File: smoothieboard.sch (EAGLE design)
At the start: 235 parts, among them IC10 LM1117-3.3V, IC2 A4982, IC3 A4982, IC4 MCP44X1, IC5 A4982, IC6 A4982, IC9 78L12Z, J10 POWER_JACKSMD, J5 POWER_JACKSMD, Q1 BC857ALT1SMD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

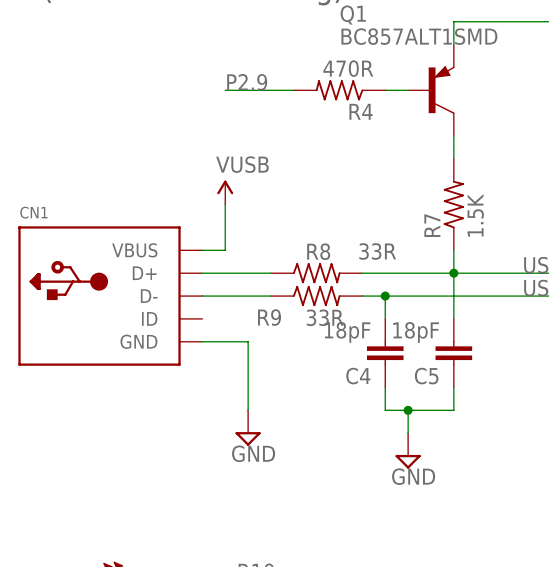
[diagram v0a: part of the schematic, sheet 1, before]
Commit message: Added USB-B Connector, other fixes
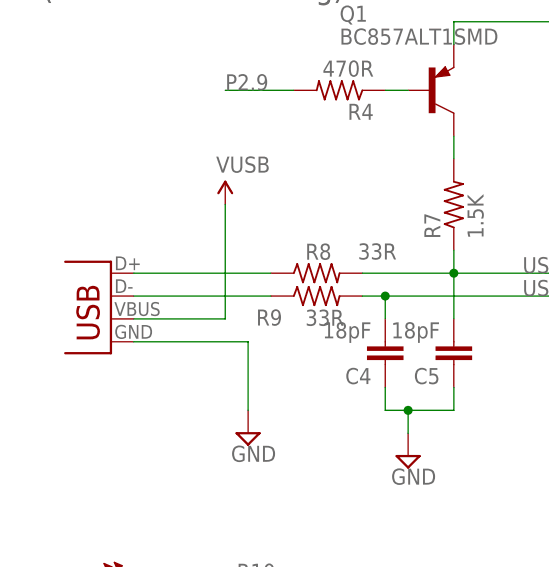
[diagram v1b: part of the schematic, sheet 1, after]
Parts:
- removed CN1: (no value), microbuilder:USBMINIB
- added X13: USBPTH, SparkFun:USBPTH
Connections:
- net GND: now also X13.GND; no longer CN1.GND
- net N$61: now also X13.D+; no longer CN1.D+
- net N$62: now also X13.D-; no longer CN1.D-
- net VUSB: now also X13.VBUS; no longer CN1.VBUS
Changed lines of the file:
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@@
 <setting verticaltext="up"/>
 </settings>
-<grid distance="0.01" unitdist="inch" unit="inch" style="lines" multiple="1" display="no" altdistance="0.01" altunitdist="inch" altunit="inch"/>
+<grid distance="0.1" unitdist="inch" unit="inch" style="lines" multiple="1" display="no" altdistance="0.01" altunitdist="inch" altunit="inch"/>
 <layers>
 <layer number="1" name="Top" color="4" fill="1" visible="no" active="no"/>
@@
 <part name="SUPPLY3" library="supply2" deviceset="GND" device=""/>
 <part name="C7" library="SparkFun" deviceset="CAP_POL" device="1206" value="10uF"/>
-<part name="CN1" library="microbuilder" deviceset="USB" device="MINIB"/>
 <part name="L1" library="SparkFun" deviceset="INDUCTOR" device="0603"/>
 <part name="SUPPLY25" library="supply2" deviceset="GND" device=""/>
@@
 <part name="JP31" library="SparkFun" deviceset="JUMPER-2" device="SMD-NC"/>
 <part name="U$2" library="custom_esorensen" deviceset="TC4427" device=""/>
+<part name="X13" library="SparkFun" deviceset="USB" device="PTH"/>
 </parts>
 <sheets>
@@
 <instance part="SUPPLY3" gate="GND" x="264.16" y="83.82"/>
 <instance part="C7" gate="G$1" x="302.26" y="96.52"/>
-<instance part="CN1" gate="G$1" x="20.32" y="149.86"/>
 <instance part="L1" gate="G$1" x="254" y="106.68" rot="R90"/>
 <instance part="SUPPLY25" gate="GND" x="226.06" y="106.68"/>
@@
 <instance part="JP15" gate="G$1" x="294.64" y="124.46" rot="R180"/>
 <instance part="JP29" gate="G$1" x="73.66" y="104.14" rot="R180"/>
+<instance part="X13" gate="G$1" x="20.32" y="144.78" rot="MR0"/>
 </instances>
 <busses>
@@
 </segment>
 <segment>
-<wire x1="30.48" y1="144.78" x2="35.56" y2="144.78" width="0.1524" layer="91"/>
 <wire x1="35.56" y1="144.78" x2="35.56" y2="137.16" width="0.1524" layer="91"/>
-<pinref part="CN1" gate="G$1" pin="GND"/>
 <pinref part="SUPPLY28" gate="GND" pin="GND"/>
+<pinref part="X13" gate="G$1" pin="GND"/>
+<wire x1="35.56" y1="144.78" x2="22.86" y2="144.78" width="0.1524" layer="91"/>
 </segment>
 <segment>
@@
 <net name="N$61" class="0">
 <segment>
-<wire x1="38.1" y1="152.4" x2="30.48" y2="152.4" width="0.1524" layer="91"/>
 <pinref part="R8" gate="G$1" pin="1"/>
-<pinref part="CN1" gate="G$1" pin="D+"/>
+<pinref part="X13" gate="G$1" pin="D+"/>
+<wire x1="22.86" y1="152.4" x2="38.1" y2="152.4" width="0.1524" layer="91"/>
 </segment>
 </net>
 <net name="N$62" class="0">
 <segment>
-<wire x1="38.1" y1="149.86" x2="30.48" y2="149.86" width="0.1524" layer="91"/>
 <pinref part="R9" gate="G$1" pin="1"/>
-<pinref part="CN1" gate="G$1" pin="D-"/>
+<pinref part="X13" gate="G$1" pin="D-"/>
+<wire x1="22.86" y1="149.86" x2="38.1" y2="149.86" width="0.1524" layer="91"/>
 </segment>
 </net>
@@
 <net name="VUSB" class="0">
 <segment>
-<wire x1="30.48" y1="154.94" x2="33.02" y2="154.94" width="0.1524" layer="91"/>
-<wire x1="33.02" y1="154.94" x2="33.02" y2="160.02" width="0.1524" layer="91"/>
 <pinref part="VUSB" gate="G$1" pin="5V"/>
-<pinref part="CN1" gate="G$1" pin="VBUS"/>
-</segment>
-</net>
+<wire x1="33.02" y1="160.02" x2="33.02" y2="147.32" width="0.1524" layer="91"/>
+<pinref part="X13" gate="G$1" pin="VBUS"/>
+<wire x1="33.02" y1="147.32" x2="22.86" y2="147.32" width="0.1524" layer="91"/>
+</segment>
+</net>

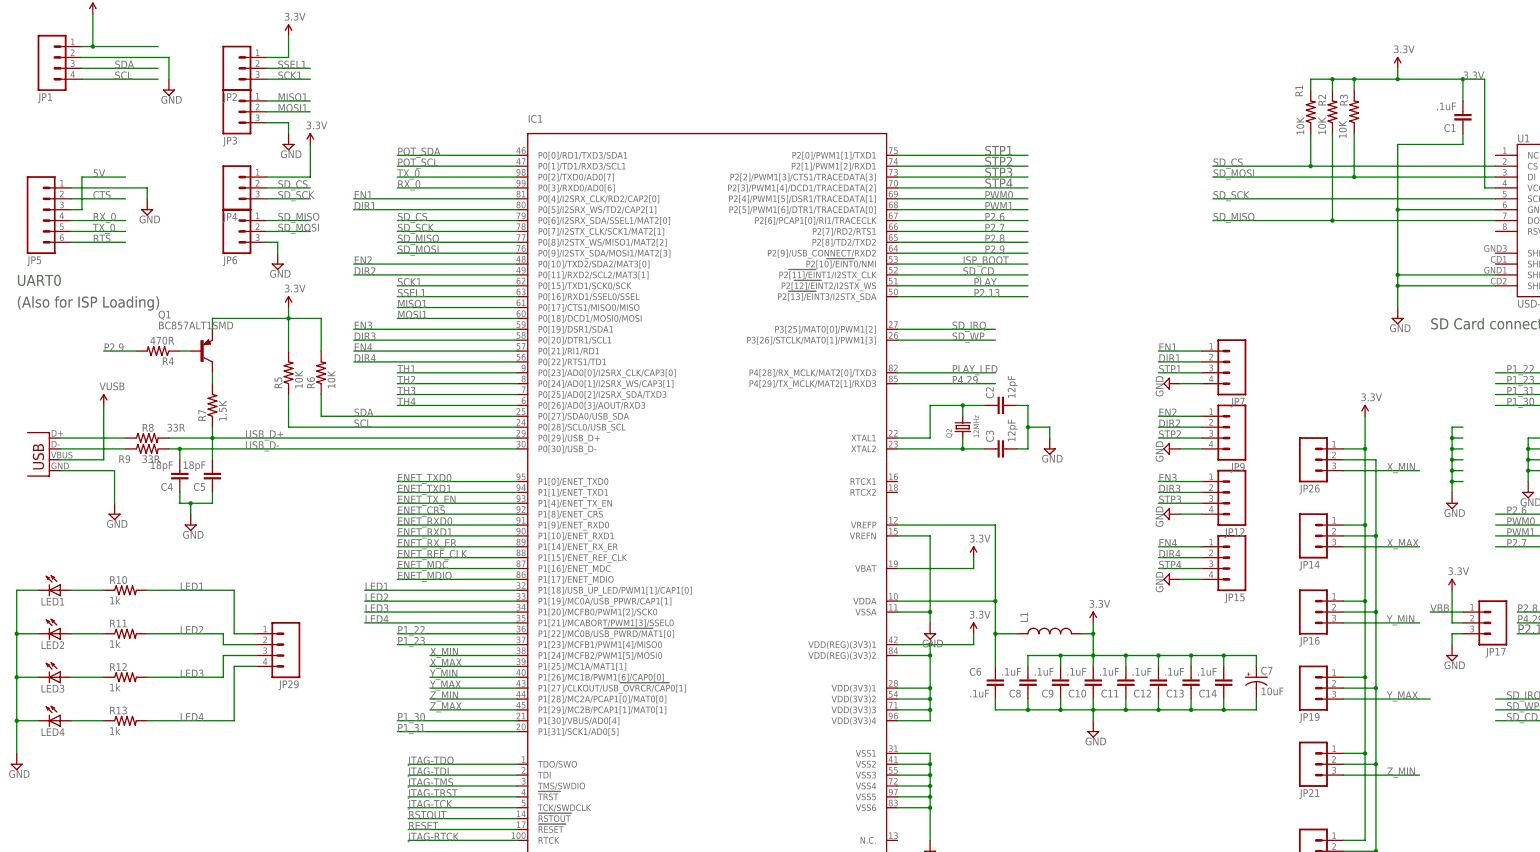
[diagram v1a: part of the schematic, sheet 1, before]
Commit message: lots of board cleanup:
removed thermals on high currenta ares

HEAPS of trace simplification

shrink 3v3 plane, use space for other signals

bulk up many polygons, use ranks to prevent shorts

separate analog ground, connect thermistors to AVCC/AGND

make trace angles 45 degrees

broken polygons connected

heaps of other fixes

changes to schematic:

thermistors connected to AGND/AVCC
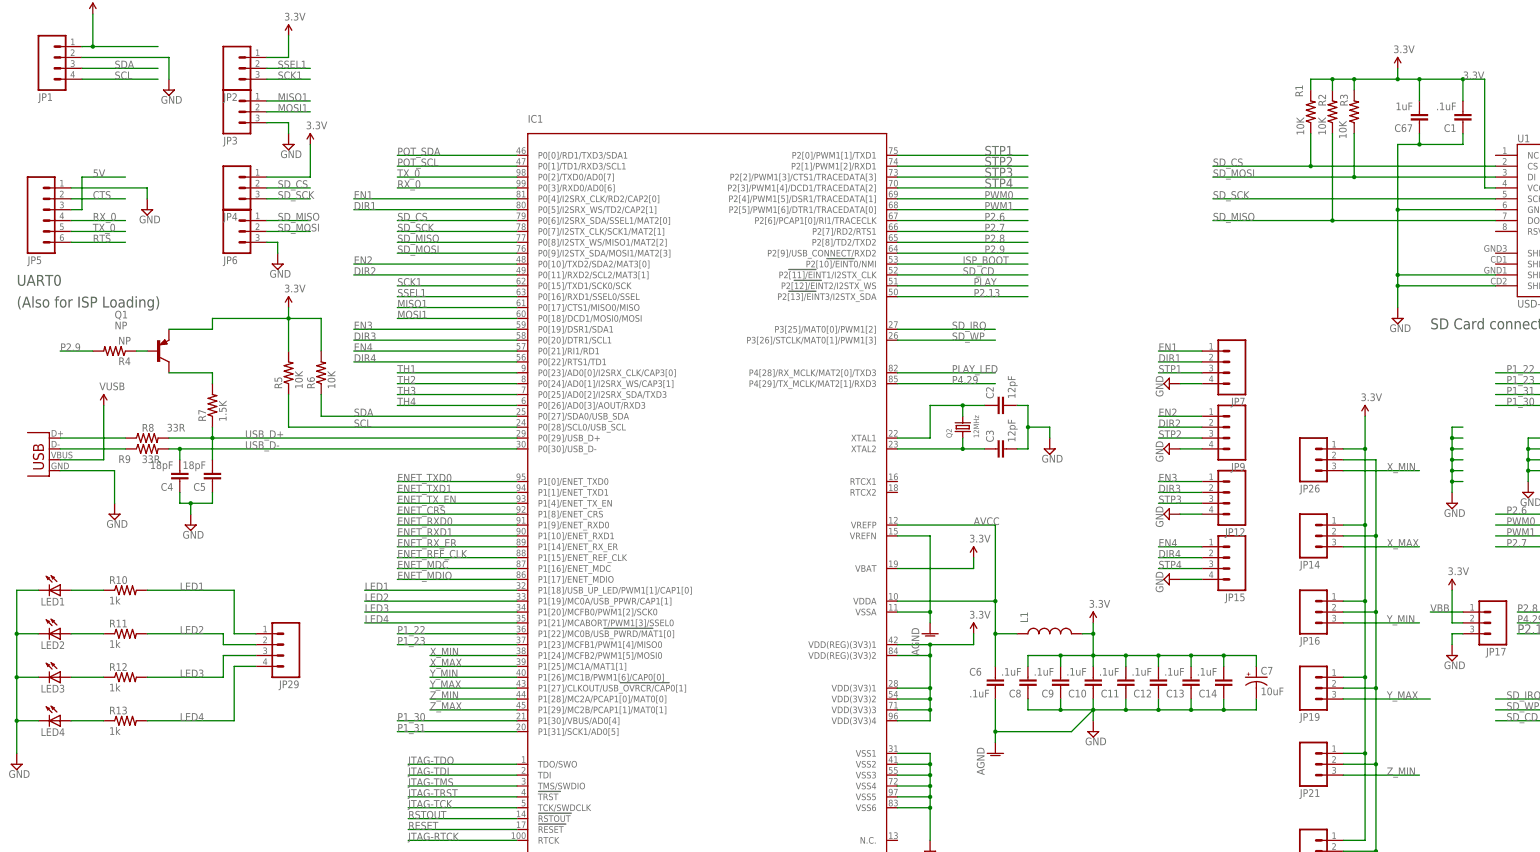
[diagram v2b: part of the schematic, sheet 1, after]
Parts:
- added C67: 1uF, resistor:C-EUC0805
- Q1: value BC857ALT1SMD -> NP
- R4: value 470R -> NP
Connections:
- net N$115 renamed 12VREG
- removed net N$18 (its old number): C6.1, IC1.VDDA, IC1.VREFP, L1.1
- new net AGND: C21.-, C22.-, C23.-, C24.-, C6.2, IC1.VREFN, IC1.VSSA, SL1.1, SL1.3, SL1.5, SL1.7
- new net AVCC: C6.1, IC1.VDDA, IC1.VREFP, L1.1, RN1A.1, RN1B.1, RN1C.1, RN1D.1
- net 3.3V: now also C67.2; no longer RN1A.1, RN1B.1, RN1C.1, RN1D.1
- net GND: now also C67.1; no longer C21.-, C22.-, C23.-, C24.-, C6.2, IC1.VREFN, IC1.VSSA, SL1.1, SL1.3, SL1.5, SL1.7
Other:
- moved on the sheet: Q1, R4

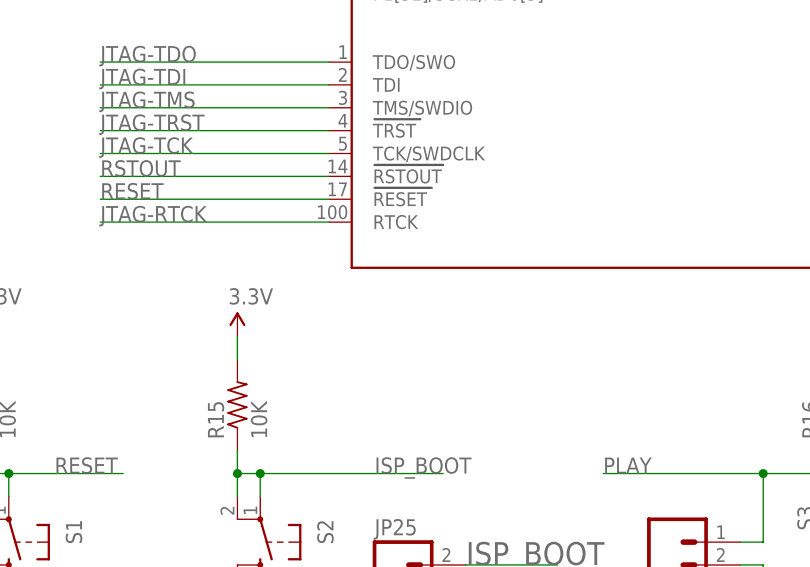
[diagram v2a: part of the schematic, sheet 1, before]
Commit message: give main IC value of LPC1769 to ease BOM generation
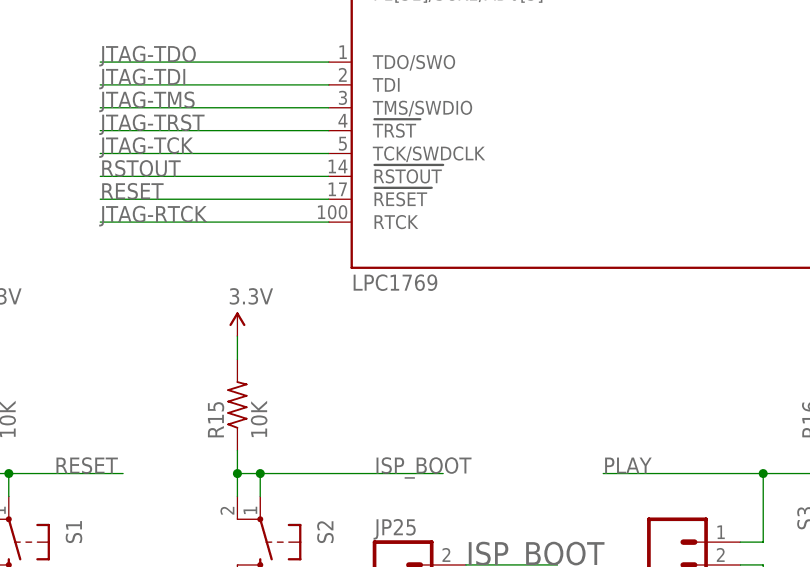
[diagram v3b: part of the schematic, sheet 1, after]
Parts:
- IC1: value (none) -> LPC1769
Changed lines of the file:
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@@
 <parts>
 <part name="FRAME2" library="microbuilder" deviceset="FRAME_A3" device=""/>
-<part name="IC1" library="microbuilder" deviceset="LPC1768" device=""/>
+<part name="IC1" library="microbuilder" deviceset="LPC1768" device="" value="LPC1769"/>
 <part name="Q2" library="microbuilder" deviceset="CRYSTAL" device="THIN" value="12MHz"/>
 <part name="C2" library="rcl" deviceset="C-EU" device="C0603" value="12pF"/>
